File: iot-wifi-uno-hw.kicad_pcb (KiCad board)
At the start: 2 copper layers, 68.6 x 53.3 mm, 62 parts, among them CON1 BARREL_JACK, P1 CONN_01X08, P2 CONN_01X08, P3 CONN_01X06, P4 CONN_01X10, P5 CONN_01X04, Q1 Q_NPN_CBE, Q2 Q_NPN_CBE, U1 usb_mini_b, U2 BD00GA5WEFJ, U3 MCP16311-MNY, U4 CH340G, U5 ESP-12E, U6 MCP6001R, U7 MOSFET-P, X1 CRYSTAL_ABM3C

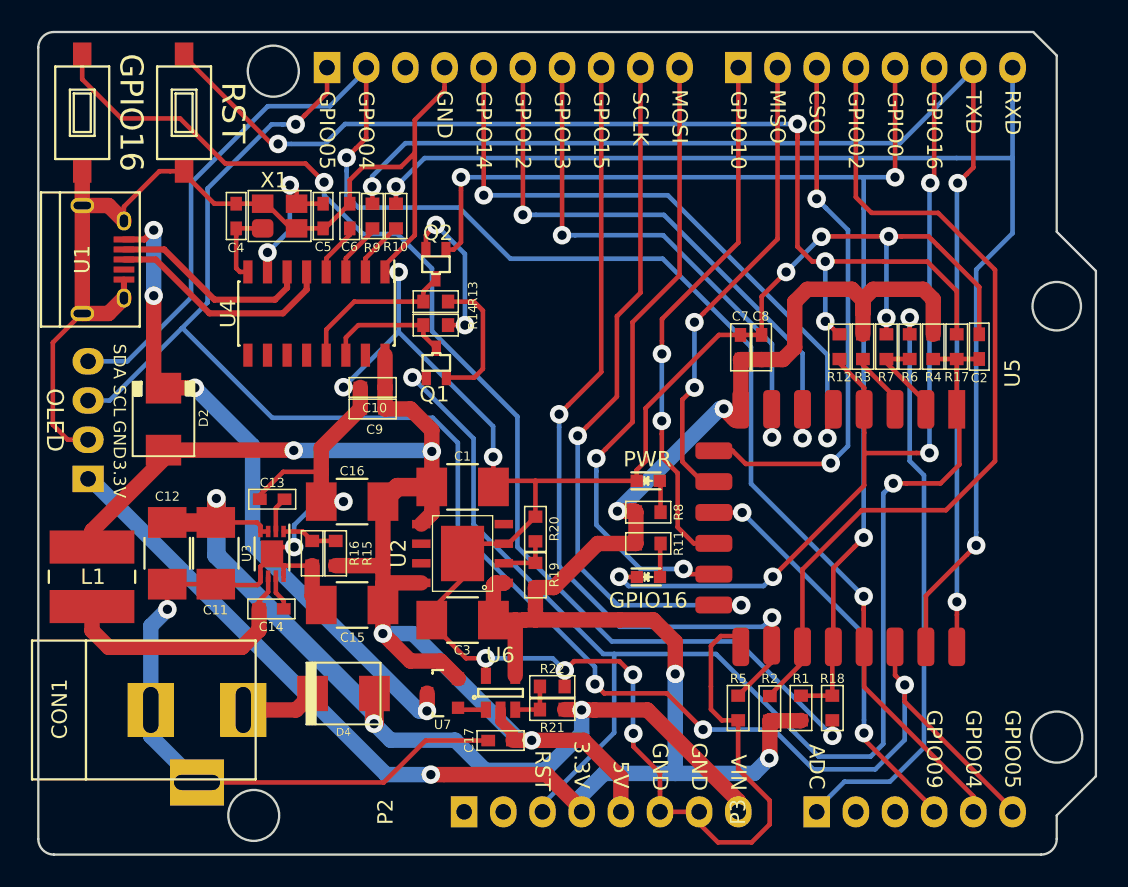
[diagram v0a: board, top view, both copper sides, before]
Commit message: modify track & silk
- rotate label same heading with component
- move some track
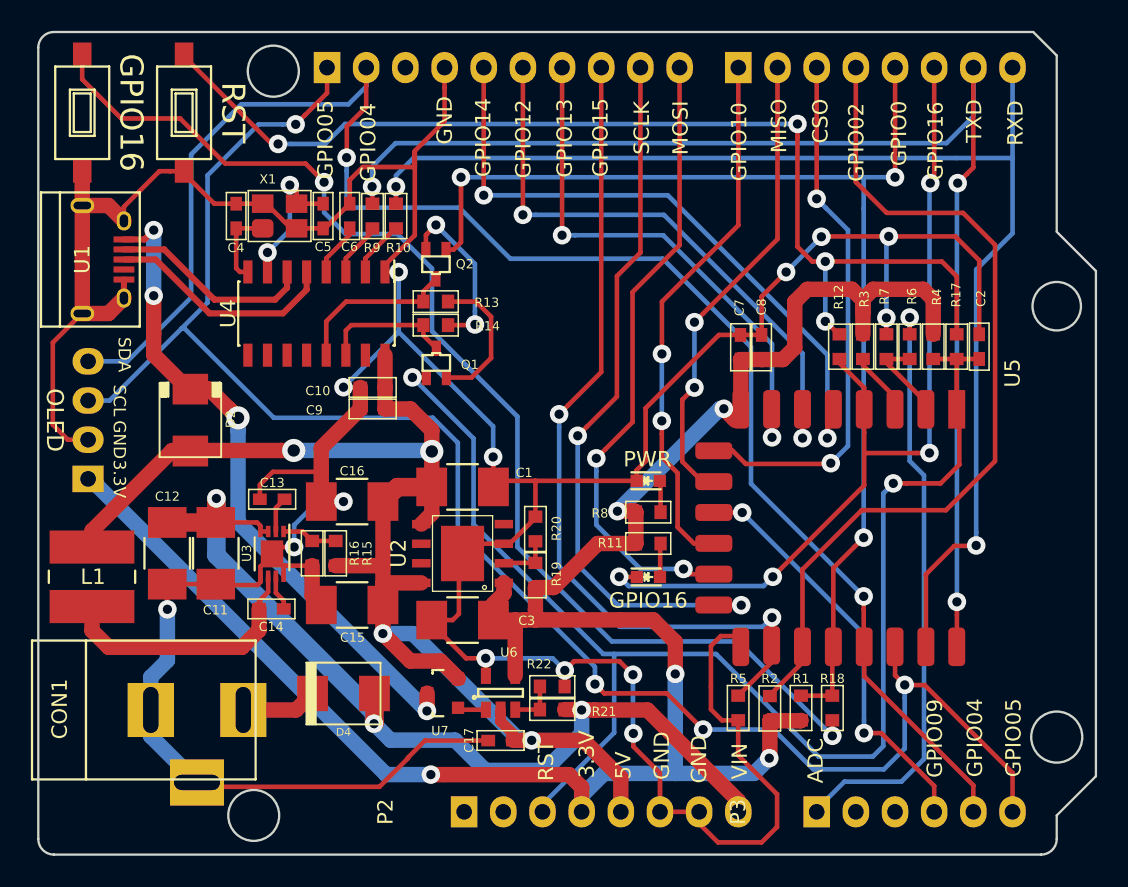
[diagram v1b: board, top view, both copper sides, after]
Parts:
- moved D2 1.75 mm to (119.4, 83.8)
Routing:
- net GND: track 284.9 -> 288.7 mm
- net TXD: track 81.1 -> 83.2 mm
- net GPIO4: track 105.6 -> 107.6 mm
- net GPIO5: track 111.3 -> 112.9 mm
- net RXD: track 81.0 -> 82.3 mm
- net Net-(Q2-Pad2): track 10.2 -> 11.1 mm
- net GPIO09: track 26.4 -> 27.1 mm
- net Net-(GPIO0-Pad1): track 76.8 -> 77.4 mm
- net Net-(R12-Pad2): track 70.2 -> 70.8 mm
- net +3V3: track 137.6 -> 138.2 mm
